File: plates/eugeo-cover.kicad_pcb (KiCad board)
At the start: 2 copper layers, 284.9 x 75.4 mm, 0 parts

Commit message: Add centre component cover
Lumberjack-style 2 mm acrylic cover over the diode stacks, MCU and USB-C,
held by four M2 10 mm standoffs. Adds mounting holes H9-H12 to the PCB
(rerouted, DRC clean, 49/49 functional checks), cover outline/DXF/gerbers,
a STEP/STL model, and a clearance check against parts and the case.

Co-Authored-By: Claude Opus 5.5 <noreply@anthropic.com>
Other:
- board size 284.9 x 75.4 mm -> 56.2 x 75.4 mm
- board text removed: "eugeo rev1.0"
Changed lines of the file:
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@@
 	)
 	(net 0 "")
+	(gr_circle
+		(center 165.4 121.6)
+		(end 166.5 121.6)
+		(stroke
+			(width 0.1)
+			(type default)
+		)
+		(fill no)
+		(layer "Edge.Cuts")
+	)
+	(gr_arc
+		(start 180.5 127.544)
+		(mid 179.62132 129.66532)
+		(end 177.5 130.544)
+		(stroke
+			(width 0.1)
+			(type default)
+		)
+		(layer "Edge.Cuts")
+	)
 	(gr_line
-		(start 294.85 56.194)
-		(end 294.85 129.544)
+		(start 127.3 55.194)
+		(end 177.5 55.194)
+		(stroke
+			(width 0.1)
+			(type default)
+		)
+		(layer "Edge.Cuts")
+	)
+	(gr_arc
+		(start 177.5 55.194)
+		(mid 179.62132 56.07268)
+		(end 180.5 58.194)
 		(stroke
 			(width 0.1)
@@
 	)
 	(gr_circle
-		(center 28.575 73.819)
-		(end 29.675 73.819)
+		(center 131.5 59.4)
+		(end 132.6 59.4)
 		(stroke
 			(width 0.1)
@@
 	)
 	(gr_circle
-		(center 276.225 111.919)
-		(end 277.325 111.919)
+		(center 173.3 59.4)
+		(end 174.4 59.4)
 		(stroke
 			(width 0.1)
@@
 	)
 	(gr_circle
-		(center 104.775 111.919)
-		(end 105.875 111.919)
+		(center 139.4 121.6)
+		(end 140.5 121.6)
 		(stroke
 			(width 0.1)
@@
 	)
 	(gr_line
-		(start 9.95 129.544)
-		(end 9.95 56.194)
+		(start 177.5 130.544)
+		(end 127.3 130.544)
 		(stroke
 			(width 0.1)
@@
 		(layer "Edge.Cuts")
 	)
-	(gr_circle
-		(center 200.025 73.819)
-		(end 201.125 73.819)
-		(stroke
-			(width 0.1)
-			(type default)
-		)
-		(fill no)
-		(layer "Edge.Cuts")
-	)
-	(gr_circle
-		(center 276.225 73.819)
-		(end 277.325 73.819)
-		(stroke
-			(width 0.1)
-			(type default)
-		)
-		(fill no)
-		(layer "Edge.Cuts")
-	)
 	(gr_arc
-		(start 9.95 56.194)
-		(mid 10.242893 55.486893)
-		(end 10.95 55.194)
-		(stroke
-			(width 0.1)
-			(type default)
-		)
-		(layer "Edge.Cuts")
-	)
-	(gr_circle
-		(center 200.025 111.919)
-		(end 201.125 111.919)
-		(stroke
-			(width 0.1)
-			(type default)
-		)
-		(fill no)
-		(layer "Edge.Cuts")
-	)
-	(gr_arc
-		(start 10.95 130.544)
-		(mid 10.242893 130.251107)
-		(end 9.95 129.544)
-		(stroke
-			(width 0.1)
-			(type default)
-		)
-		(layer "Edge.Cuts")
-	)
-	(gr_circle
-		(center 104.775 73.819)
-		(end 105.875 73.819)
-		(stroke
-			(width 0.1)
-			(type default)
-		)
-		(fill no)
-		(layer "Edge.Cuts")
-	)
-	(gr_line
-		(start 10.95 55.194)
-		(end 293.85 55.194)
+		(start 124.3 58.194)
+		(mid 125.17868 56.07268)
+		(end 127.3 55.194)
 		(stroke
 			(width 0.1)
@@
 	)
 	(gr_line
-		(start 293.85 130.544)
-		(end 10.95 130.544)
+		(start 180.5 58.194)
+		(end 180.5 127.544)
 		(stroke
 			(width 0.1)
@@
 	)
 	(gr_arc
-		(start 293.85 55.194)
-		(mid 294.557107 55.486893)
-		(end 294.85 56.194)
+		(start 127.3 130.544)
+		(mid 125.17868 129.66532)
+		(end 124.3 127.544)
 		(stroke
 			(width 0.1)
@@
 		(layer "Edge.Cuts")
 	)
-	(gr_circle
-		(center 28.575 111.919)
-		(end 29.675 111.919)
-		(stroke
-			(width 0.1)
-			(type default)
-		)
-		(fill no)
-		(layer "Edge.Cuts")
-	)
-	(gr_arc
-		(start 294.85 129.544)
-		(mid 294.557107 130.251107)
-		(end 293.85 130.544)
+	(gr_line
+		(start 124.3 127.544)
+		(end 124.3 58.194)
 		(stroke
 			(width 0.1)
@@
 		(layer "Edge.Cuts")
 	)
-	(gr_text "eugeo rev1.0"
-		(at 152.4 92.869 0)
-		(layer "F.SilkS")
-		(effects
-			(font
-				(size 1.2 1.2)
-				(thickness 0.18)
-			)
-		)
-	)
 	(embedded_fonts no)

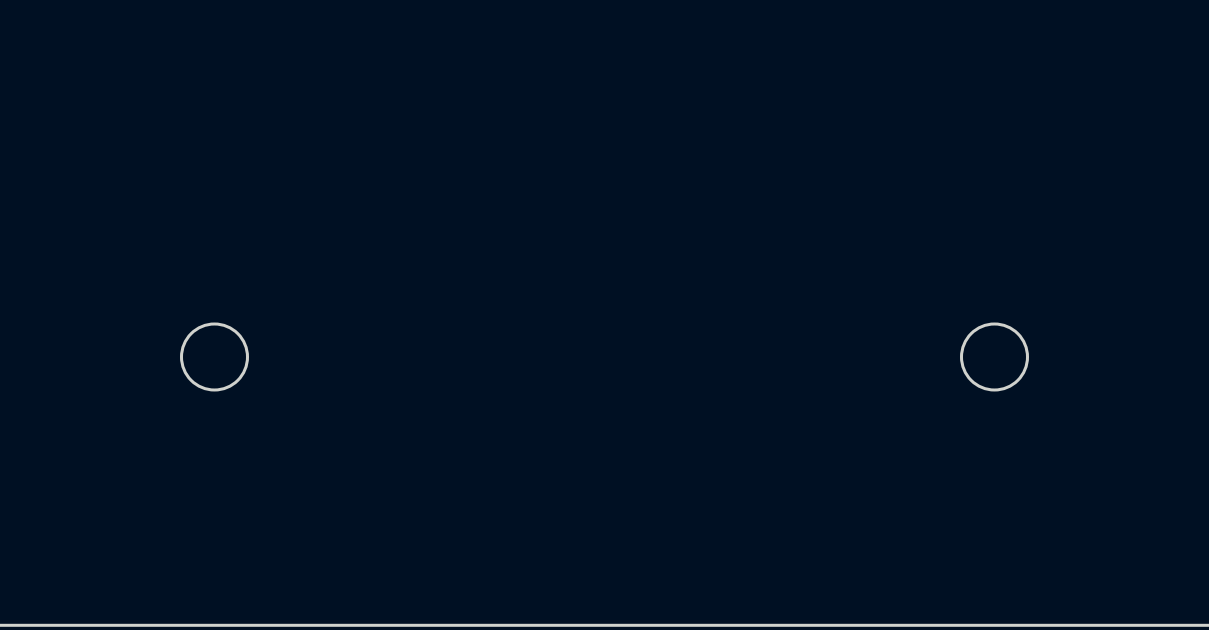
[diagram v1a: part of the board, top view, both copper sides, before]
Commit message: Switch to RP2040, zigzag diodes and a frozen-stump back
- MCU: ATmega328P + V-USB -> RP2040 + W25Q16 QSPI flash, 12 MHz crystal,
  MCP1700 3.3 V LDO, USBLC6 ESD and 27R series resistors. SMD parts are
  assembled by JLCPCB (BOM/CPL now include them); everything else stays
  through-hole and on show.
- RP2040 block is hand-routed: +3V3 ring inside the pin ring, +1V1 via the
  back, QSPI / crystal / decoupling / row and column escapes. ISP and SWD
  headers dropped (UF2 flashing over USB with BOOT + RESET).
- Diode stacks zigzag like Lumberjack.
- Back side artwork: frozen tree stump with frost ferns and snowflakes,
  some as bare-copper mask openings (scripts/stump_art.py).
- QMK: RP2040 / rp2040 bootloader, new GP pin map, prebuilt UF2 files.
- verify_design.py rewritten for RP2040 (59 checks), preorder checks 23/23.
- Case support pillar moved clear of U4; cover, plates and laser-cut SVGs
  regenerated for the new cover holes.

Co-Authored-By: Claude Opus 5.5 <noreply@anthropic.com>
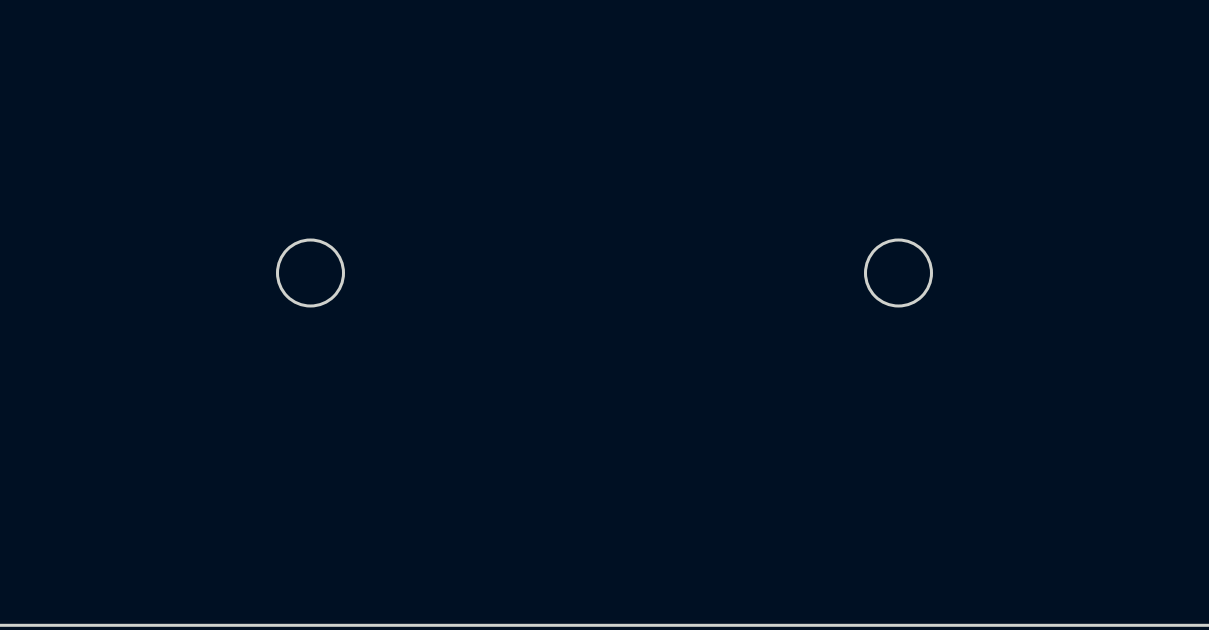
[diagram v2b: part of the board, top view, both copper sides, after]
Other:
- outline, holes or cut-outs redrawn
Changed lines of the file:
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@@
 	)
 	(net 0 "")
+	(gr_line
+		(start 180.5 58.194)
+		(end 180.5 127.544)
+		(stroke
+			(width 0.1)
+			(type default)
+		)
+		(layer "Edge.Cuts")
+	)
+	(gr_line
+		(start 177.5 130.544)
+		(end 127.3 130.544)
+		(stroke
+			(width 0.1)
+			(type default)
+		)
+		(layer "Edge.Cuts")
+	)
+	(gr_line
+		(start 124.3 127.544)
+		(end 124.3 58.194)
+		(stroke
+			(width 0.1)
+			(type default)
+		)
+		(layer "Edge.Cuts")
+	)
 	(gr_circle
-		(center 165.4 121.6)
-		(end 166.5 121.6)
+		(center 131.5 59.4)
+		(end 132.6 59.4)
+		(stroke
+			(width 0.1)
+			(type default)
+		)
+		(fill no)
+		(layer "Edge.Cuts")
+	)
+	(gr_line
+		(start 127.3 55.194)
+		(end 177.5 55.194)
+		(stroke
+			(width 0.1)
+			(type default)
+		)
+		(layer "Edge.Cuts")
+	)
+	(gr_circle
+		(center 173.3 59.4)
+		(end 174.4 59.4)
 		(stroke
 			(width 0.1)
@@
 	)
 	(gr_arc
-		(start 180.5 127.544)
-		(mid 179.62132 129.66532)
-		(end 177.5 130.544)
-		(stroke
-			(width 0.1)
-			(type default)
-		)
-		(layer "Edge.Cuts")
-	)
-	(gr_line
-		(start 127.3 55.194)
-		(end 177.5 55.194)
+		(start 127.3 130.544)
+		(mid 125.17868 129.66532)
+		(end 124.3 127.544)
 		(stroke
 			(width 0.1)
@@
 		(layer "Edge.Cuts")
 	)
-	(gr_circle
-		(center 131.5 59.4)
-		(end 132.6 59.4)
-		(stroke
-			(width 0.1)
-			(type default)
-		)
-		(fill no)
-		(layer "Edge.Cuts")
-	)
-	(gr_circle
-		(center 173.3 59.4)
-		(end 174.4 59.4)
-		(stroke
-			(width 0.1)
-			(type default)
-		)
-		(fill no)
-		(layer "Edge.Cuts")
-	)
-	(gr_circle
-		(center 139.4 121.6)
-		(end 140.5 121.6)
-		(stroke
-			(width 0.1)
-			(type default)
-		)
-		(fill no)
-		(layer "Edge.Cuts")
-	)
-	(gr_line
-		(start 177.5 130.544)
-		(end 127.3 130.544)
-		(stroke
-			(width 0.1)
-			(type default)
-		)
-		(layer "Edge.Cuts")
-	)
 	(gr_arc
 		(start 124.3 58.194)
@@
 		(layer "Edge.Cuts")
 	)
-	(gr_line
-		(start 180.5 58.194)
-		(end 180.5 127.544)
+	(gr_arc
+		(start 180.5 127.544)
+		(mid 179.62132 129.66532)
+		(end 177.5 130.544)
 		(stroke
 			(width 0.1)
@@
 		(layer "Edge.Cuts")
 	)
-	(gr_arc
-		(start 127.3 130.544)
-		(mid 125.17868 129.66532)
-		(end 124.3 127.544)
+	(gr_circle
+		(center 142.6 118.8)
+		(end 143.7 118.8)
 		(stroke
 			(width 0.1)
 			(type default)
 		)
+		(fill no)
 		(layer "Edge.Cuts")
 	)
-	(gr_line
-		(start 124.3 127.544)
-		(end 124.3 58.194)
+	(gr_circle
+		(center 162.2 118.8)
+		(end 163.299999 118.8)
 		(stroke
 			(width 0.1)
 			(type default)
 		)
+		(fill no)
 		(layer "Edge.Cuts")
 	)

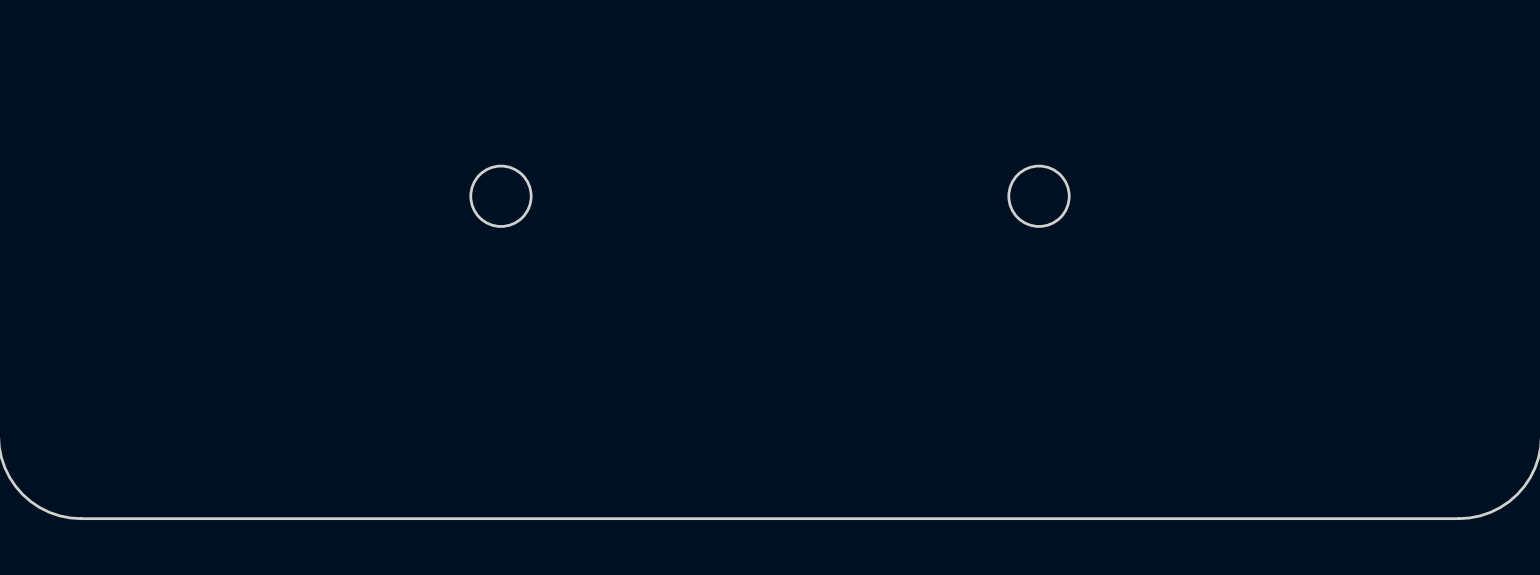
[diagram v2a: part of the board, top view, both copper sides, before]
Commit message: Cover screws at the corners and a large EUGEO logo on the back
- Centre cover holes move to the four corners of the acrylic
  (131.5 / 173.3 x 59.4 / 126.3). The column buses along the bottom edge
  split around the lower screws: COL5 / COL4 above, COL3..COL0 below.
- Back side: Futura "EUGEO" (same face as the case nameplate), 7.5 mm cap
  height with a rule and dot each side, in the free band between key rows
  1 and 2. Letters are pre-outlined by scripts/logo_outline.py into
  scripts/logo_eugeo.json and drawn by stump_art.py, which keeps the frost
  and snowflakes clear of it.
- Cover, plates, laser-cut SVGs, case and renders regenerated.

Co-Authored-By: Claude Opus 5.5 <noreply@anthropic.com>
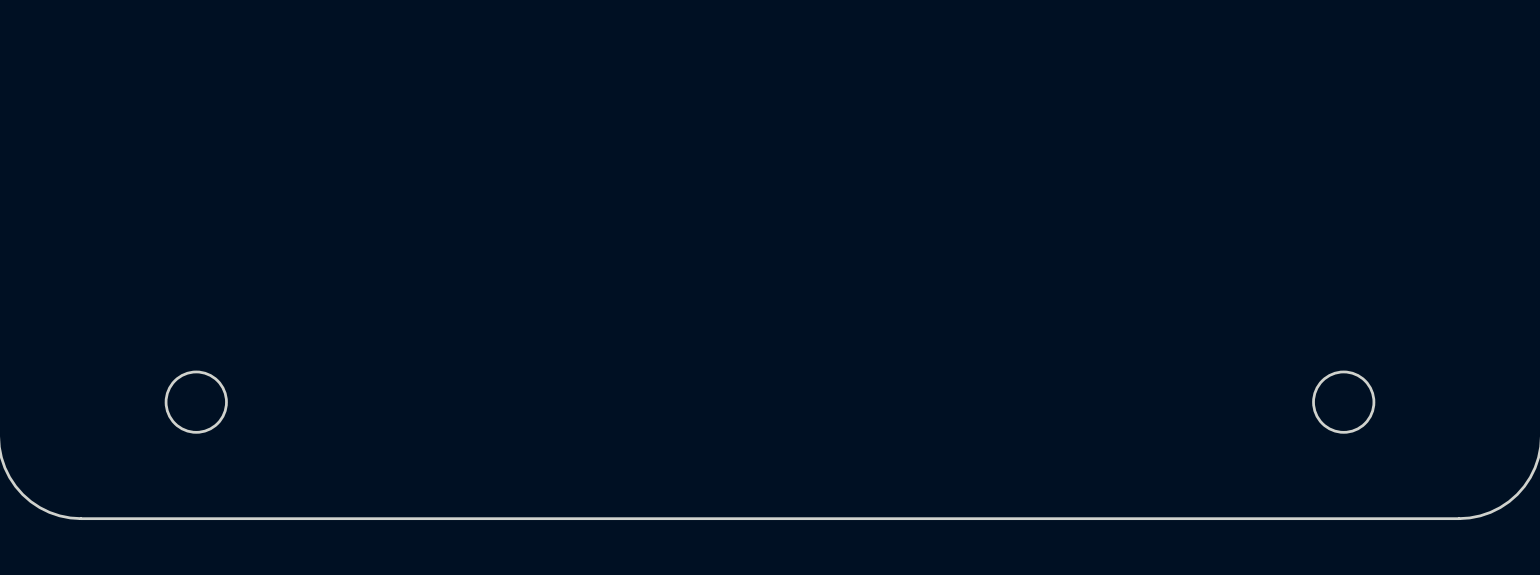
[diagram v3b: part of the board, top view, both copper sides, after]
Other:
- outline, holes or cut-outs redrawn
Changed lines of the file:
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@@
 	)
 	(net 0 "")
-	(gr_line
-		(start 180.5 58.194)
-		(end 180.5 127.544)
+	(gr_circle
+		(center 173.3 59.4)
+		(end 174.4 59.4)
 		(stroke
 			(width 0.1)
 			(type default)
 		)
+		(fill no)
+		(layer "Edge.Cuts")
+	)
+	(gr_arc
+		(start 177.5 55.194)
+		(mid 179.62132 56.07268)
+		(end 180.5 58.194)
+		(stroke
+			(width 0.1)
+			(type default)
+		)
+		(layer "Edge.Cuts")
+	)
+	(gr_circle
+		(center 173.3 126.3)
+		(end 174.4 126.3)
+		(stroke
+			(width 0.1)
+			(type default)
+		)
+		(fill no)
+		(layer "Edge.Cuts")
+	)
+	(gr_circle
+		(center 131.5 59.4)
+		(end 132.6 59.4)
+		(stroke
+			(width 0.1)
+			(type default)
+		)
+		(fill no)
 		(layer "Edge.Cuts")
 	)
@@
 		(layer "Edge.Cuts")
 	)
-	(gr_circle
-		(center 131.5 59.4)
-		(end 132.6 59.4)
+	(gr_arc
+		(start 124.3 58.194)
+		(mid 125.17868 56.07268)
+		(end 127.3 55.194)
 		(stroke
 			(width 0.1)
 			(type default)
 		)
-		(fill no)
 		(layer "Edge.Cuts")
 	)
@@
 	)
 	(gr_circle
-		(center 173.3 59.4)
-		(end 174.4 59.4)
+		(center 131.5 126.3)
+		(end 132.6 126.3)
 		(stroke
 			(width 0.1)
@@
 	)
 	(gr_arc
-		(start 177.5 55.194)
-		(mid 179.62132 56.07268)
-		(end 180.5 58.194)
-		(stroke
-			(width 0.1)
-			(type default)
-		)
-		(layer "Edge.Cuts")
-	)
-	(gr_arc
-		(start 124.3 58.194)
-		(mid 125.17868 56.07268)
-		(end 127.3 55.194)
-		(stroke
-			(width 0.1)
-			(type default)
-		)
-		(layer "Edge.Cuts")
-	)
-	(gr_arc
 		(start 180.5 127.544)
 		(mid 179.62132 129.66532)
@@
 		(layer "Edge.Cuts")
 	)
-	(gr_circle
-		(center 142.6 118.8)
-		(end 143.7 118.8)
+	(gr_line
+		(start 180.5 58.194)
+		(end 180.5 127.544)
 		(stroke
 			(width 0.1)
 			(type default)
 		)
-		(fill no)
 		(layer "Edge.Cuts")
 	)
-	(gr_circle
-		(center 162.2 118.8)
-		(end 163.299999 118.8)
-		(stroke
-			(width 0.1)
-			(type default)
-		)
-		(fill no)
-		(layer "Edge.Cuts")
-	)
